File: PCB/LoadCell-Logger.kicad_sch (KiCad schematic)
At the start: 71 parts, among them CN2 LoadCell, CN3 LoadCell, CN4 LoadCell, Q2 MMBT3906, Q3 MMBT3906, Q4 MMBT3906, SW2 Reset, U1 Pico, U2 TC74HCU04AF, U3 HX711, U4 HX711, U5 HX711, U6 HX711, U7 Pico

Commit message: 部品配置
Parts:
- C1, C10, C12, C13, C15, C17, C18, C20, C22, C3, C7, C8: footprint (none) -> Capacitor_SMD:C_0603_1608Metric_Pad1.08x0.95mm_HandSolder
- C11, C14, C16, C19, C21, C9: footprint (none) -> Capacitor_SMD:C_0805_2012Metric_Pad1.18x1.45mm_HandSolder
- C2: value (none) -> 10p; footprint (none) -> Capacitor_SMD:C_0603_1608Metric_Pad1.08x0.95mm_HandSolder
- C4, C6: value (none) -> 10u; footprint (none) -> Capacitor_SMD:C_0805_2012Metric_Pad1.18x1.45mm_HandSolder
- C5: value (none) -> 0.1u; footprint (none) -> Capacitor_SMD:C_0603_1608Metric_Pad1.08x0.95mm_HandSolder
- CN1: value (none) -> LoadCell; footprint (none) -> Connector_Molex:Molex_SPOX_5268-04A_1x04_P2.50mm_Horizontal
- CN2, CN3, CN4: footprint (none) -> Connector_Molex:Molex_SPOX_5268-04A_1x04_P2.50mm_Horizontal
- D1: value (none) -> LED; footprint (none) -> LED_SMD:LED_0603_1608Metric_Pad1.05x0.95mm_HandSolder
- D2, D3, D4: footprint (none) -> LED_SMD:LED_0603_1608Metric_Pad1.05x0.95mm_HandSolder
- J1: value (none) -> Debug; footprint (none) -> user:STlink
- J2: value (none) -> Debug_Power; footprint (none) -> Connector_JST:JST_XH_S2B-XH-A_1x02_P2.50mm_Horizontal
- J3: value (none) -> Debug_XH; footprint (none) -> Connector_JST:JST_XH_S5B-XH-A_1x05_P2.50mm_Horizontal
- L1: value (none) -> BLM18RK102; footprint (none) -> Inductor_SMD:L_0603_1608Metric_Pad1.05x0.95mm_HandSolder
- Q1: value (none) -> MMBT3906; footprint (none) -> Package_TO_SOT_SMD:SOT-23
- R1: footprint (none) -> Resistor_SMD:R_0805_2012Metric_Pad1.20x1.40mm_HandSolder
- R10, R11, R12, R13, R14, R15, R16, R17, R18, R20, R21, R22, R6, R7, R8, R9: footprint (none) -> Resistor_SMD:R_0603_1608Metric_Pad0.98x0.95mm_HandSolder
- R19: value (none) -> 1k; footprint (none) -> Resistor_SMD:R_0603_1608Metric_Pad0.98x0.95mm_HandSolder
- R2: value (none) -> 300; footprint (none) -> Resistor_SMD:R_0603_1608Metric_Pad0.98x0.95mm_HandSolder
- R3: value (none) -> 22k; footprint (none) -> Resistor_SMD:R_0603_1608Metric_Pad0.98x0.95mm_HandSolder
- R4: value (none) -> 10k; footprint (none) -> Resistor_SMD:R_0603_1608Metric_Pad0.98x0.95mm_HandSolder
- R5: value (none) -> 100; footprint (none) -> Resistor_SMD:R_0603_1608Metric_Pad0.98x0.95mm_HandSolder
- SW1: value (none) -> User; footprint (none) -> user:SKRPACE010_kai
- SW2: footprint (none) -> user:SKRPACE010_kai
- SW3: value (none) -> SW_SPDT; footprint (none) -> user:SSSS213202_parallel
- U1, U7: footprint (none) -> MCU_RaspberryPi_and_Boards:RPi_Pico_SMD_TH
- U2: footprint (none) -> Package_SO:SO-14_5.3x10.2mm_P1.27mm
- U3, U4, U5, U6: footprint (none) -> Package_SO:SOP-16_3.9x9.9mm_P1.27mm
- Y1: value (none) -> 13.824MHz; footprint (none) -> Crystal:Crystal_HC49-U_Vertical
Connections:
- net CLK1: now also U2.2; no longer U2.6
- net GND: now also J1.5 (Pin_5); no longer C10.2, C11.1, C14.2, C15.2, C16.1, C19.2, C20.2, C21.1, C4.2, C5.2, C6.1, C9.2, CN1.2 (Pin_2), CN2.2 (Pin_2), CN3.2 (Pin_2), CN4.2 (Pin_2), R12.2, R16.2, R4.2, R8.2, U3.5 (AGND), U4.5 (AGND), U5.5 (AGND), U6.5 (AGND)
- net at R1.2, R2.2: now also U2.4, U2.5; no longer U2.2, U2.3
- net at C1.1, R1.1, Y1.1: now also U2.3; no longer U2.1
- net at U2.11, U2.13, U2.9: now also U2.1, U2.6; no longer U2.4, U2.5
- new net GNDA: C10.2, C11.1, C14.2, C15.2, C16.1, C19.2, C20.2, C21.1, C4.2, C5.2, C6.1, C9.2, CN1.2 (Pin_2), CN2.2 (Pin_2), CN3.2 (Pin_2), CN4.2 (Pin_2), R12.2, R16.2, R4.2, R8.2, U3.5 (AGND), U4.5 (AGND), U5.5 (AGND), U6.5 (AGND)
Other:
- moved on the sheet: U2A, U2B, U2C

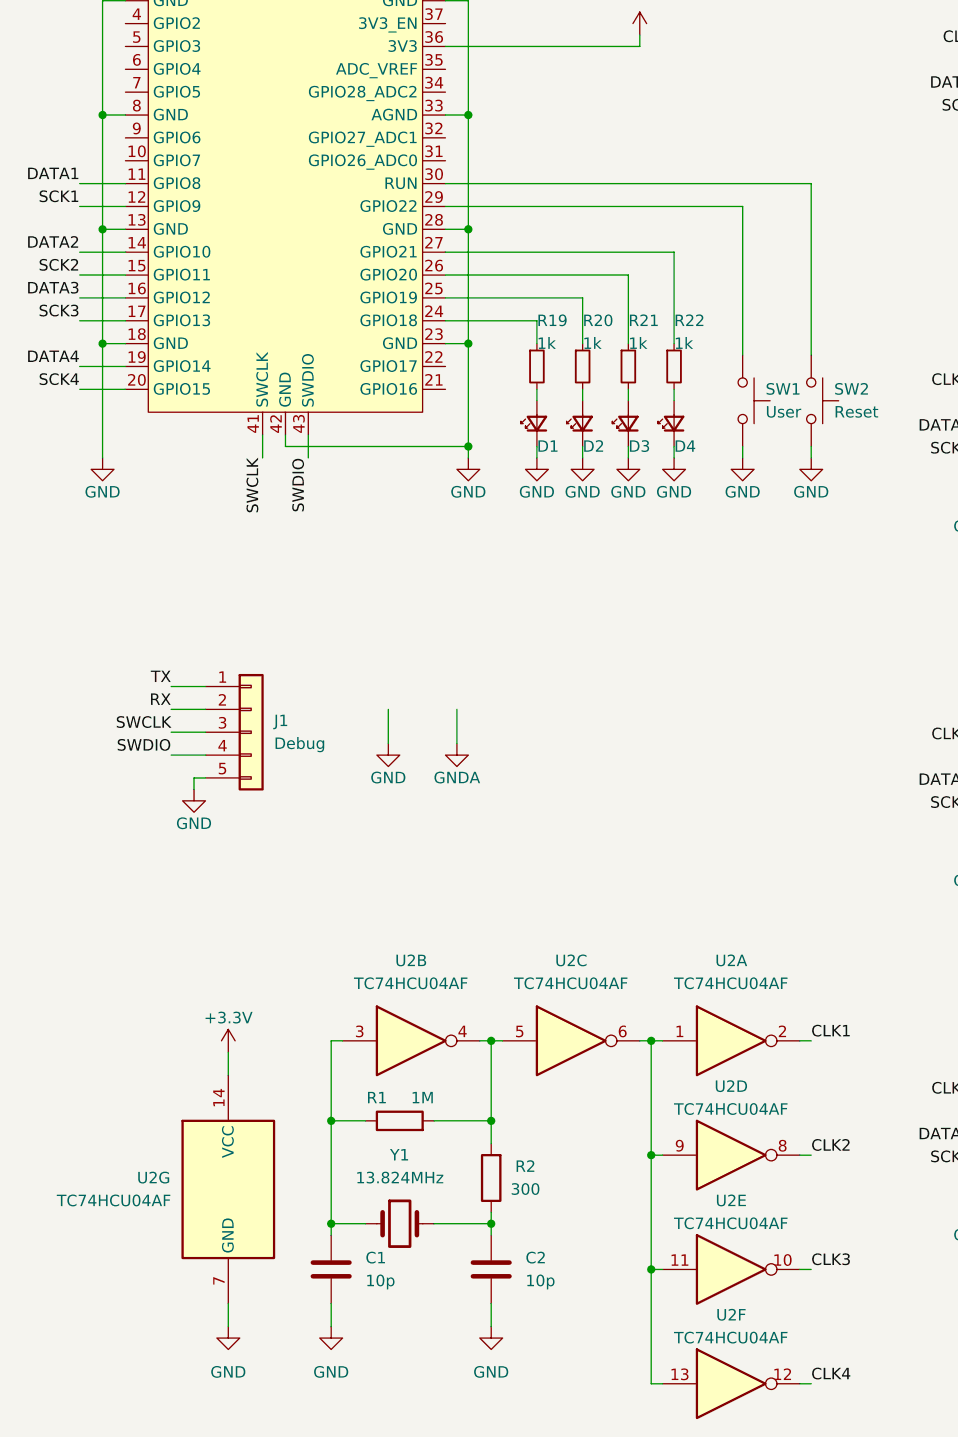
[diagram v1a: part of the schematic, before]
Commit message: ロガー側配線完了
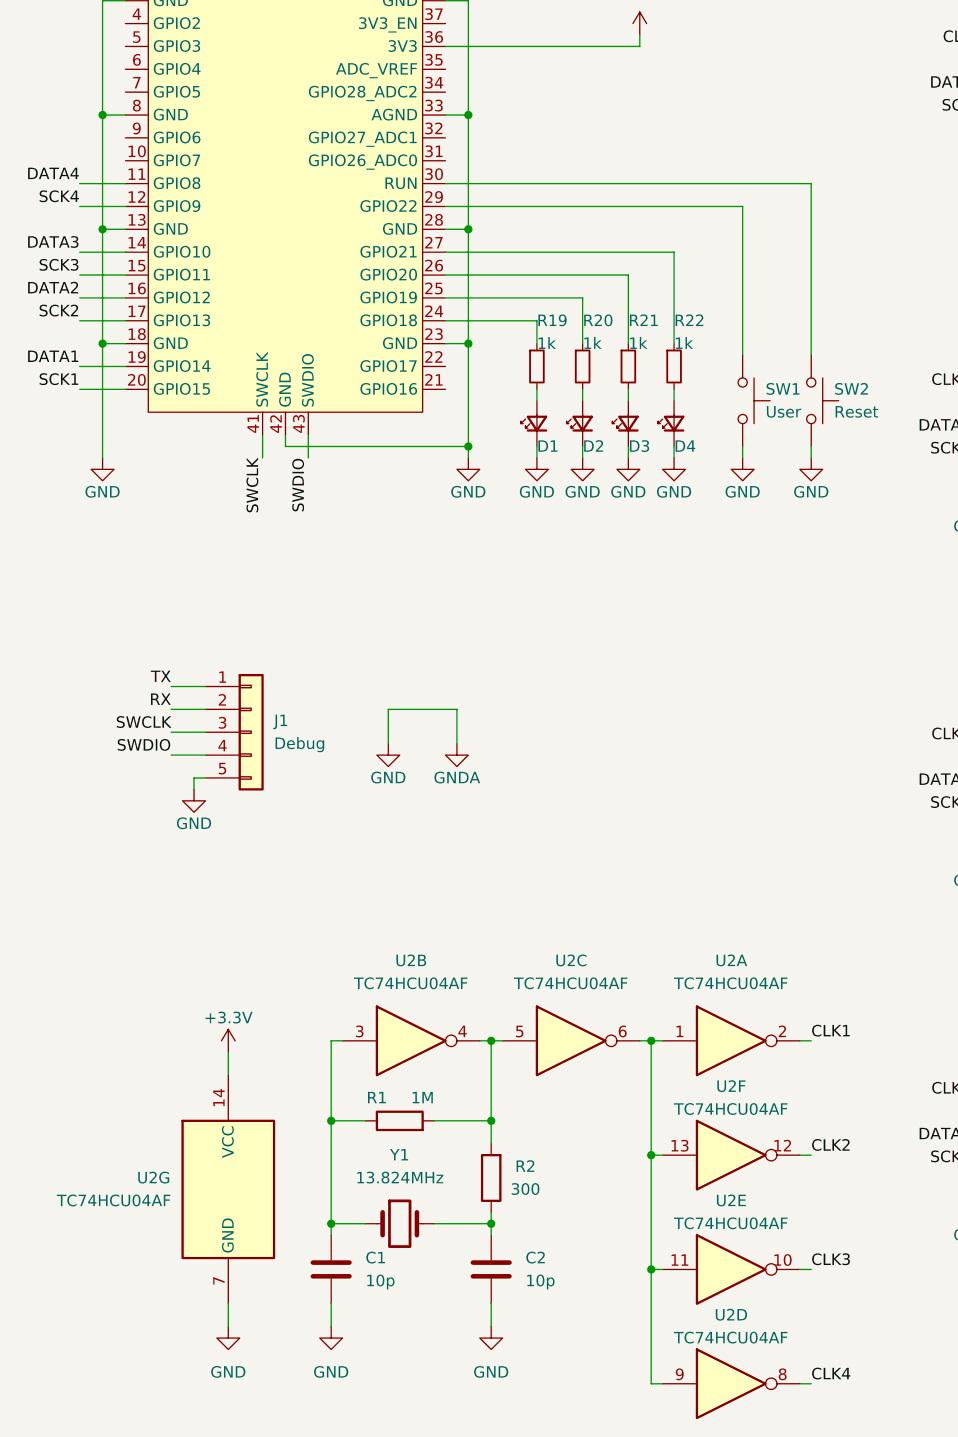
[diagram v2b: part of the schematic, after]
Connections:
- net GNDA is gone; now on net GND: C10.2, C11.1, C14.2, C15.2, C16.1, C19.2, C20.2, C21.1, C4.2, C5.2, C6.1, C9.2, CN1.2 (Pin_2), CN2.2 (Pin_2), CN3.2 (Pin_2), CN4.2 (Pin_2), R12.2, R16.2, R4.2, R8.2, U3.5 (AGND), U4.5 (AGND), U5.5 (AGND), U6.5 (AGND)
- net CLK2: now also U2.12; no longer U2.8
- net CLK4: now also U2.8; no longer U2.12
- net DATA1: now also U1.19 (GPIO14); no longer U1.11 (GPIO8)
- net DATA2: now also U1.16 (GPIO12); no longer U1.14 (GPIO10)
- net DATA3: now also U1.14 (GPIO10); no longer U1.16 (GPIO12)
- net DATA4: now also U1.11 (GPIO8); no longer U1.19 (GPIO14)
- net SCK1: now also U1.20 (GPIO15); no longer U1.12 (GPIO9)
- net SCK2: now also U1.17 (GPIO13); no longer U1.15 (GPIO11)
- net SCK3: now also U1.15 (GPIO11); no longer U1.17 (GPIO13)
- net SCK4: now also U1.12 (GPIO9); no longer U1.20 (GPIO15)
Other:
- moved on the sheet: U2D, U2F
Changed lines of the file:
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@@
+    (stroke (width 0) (type default) (color 0 0 0 0))
+  )
+  (wire (pts (xy 55.88 106.68) (xy 63.5 106.68))
     (stroke (width 0) (type default) (color 0 0 0 0))
   )
@@
     (effects (font (size 1.27 1.27)) (justify right bottom))
   )
-  (label "SCK1" (at 21.59 50.8 180)
+  (label "SCK4" (at 21.59 50.8 180)
     (effects (font (size 1.27 1.27)) (justify right bottom))
   )
@@
     (effects (font (size 1.27 1.27)) (justify right bottom))
   )
-  (label "DATA2" (at 21.59 55.88 180)
+  (label "DATA3" (at 21.59 55.88 180)
     (effects (font (size 1.27 1.27)) (justify right bottom))
   )
@@
     (effects (font (size 1.27 1.27)) (justify right bottom))
   )
-  (label "DATA4" (at 21.59 68.58 180)
+  (label "DATA1" (at 21.59 68.58 180)
     (effects (font (size 1.27 1.27)) (justify right bottom))
   )
@@
     (effects (font (size 1.27 1.27)) (justify right bottom))
   )
-  (label "SCK2" (at 21.59 58.42 180)
-    (effects (font (size 1.27 1.27)) (justify right bottom))
-  )
-  (label "SCK4" (at 21.59 71.12 180)
+  (label "SCK3" (at 21.59 58.42 180)
+    (effects (font (size 1.27 1.27)) (justify right bottom))
+  )
+  (label "SCK1" (at 21.59 71.12 180)
     (effects (font (size 1.27 1.27)) (justify right bottom))
   )
@@
     (effects (font (size 1.27 1.27)) (justify right bottom))
   )
-  (label "DATA3" (at 21.59 60.96 180)
+  (label "DATA2" (at 21.59 60.96 180)
     (effects (font (size 1.27 1.27)) (justify right bottom))
   )
@@
     (effects (font (size 1.27 1.27)) (justify right bottom))
   )
-  (label "DATA1" (at 21.59 48.26 180)
+  (label "DATA4" (at 21.59 48.26 180)
     (effects (font (size 1.27 1.27)) (justify right bottom))
   )
@@
     (effects (font (size 1.27 1.27)) (justify right bottom))
   )
-  (label "SCK3" (at 21.59 63.5 180)
+  (label "SCK2" (at 21.59 63.5 180)
     (effects (font (size 1.27 1.27)) (justify right bottom))
   )
@@
   (symbol (lib_id "power:GND") (at 34.29 115.57 0) (unit 1)
     (in_bom yes) (on_board yes)
-    (property "Reference" "#PWR?" (id 0) (at 34.29 121.92 0)
+    (property "Reference" "#PWR0101" (id 0) (at 34.29 121.92 0)
       (effects (font (size 1.27 1.27)) hide)
     )
@@
     (pin "2")
   )
-  (symbol (lib_id "74xx:74HC04") (at 93.98 181.61 0) (unit 6)
-    (in_bom yes) (on_board yes)
-    (property "Reference" "U2" (id 0) (at 93.98 173.99 0))
-    (property "Value" "TC74HCU04AF" (id 1) (at 93.98 176.53 0))
-    (property "Footprint" "Package_SO:SO-14_5.3x10.2mm_P1.27mm" (id 2) (at 93.98 181.61 0)
-      (effects (font (size 1.27 1.27)) hide)
-    )
-    (property "Datasheet" "https://assets.nexperia.com/documents/data-sheet/74HC_HCT04.pdf" (id 3) (at 93.98 181.61 0)
+  (symbol (lib_id "74xx:74HC04") (at 93.98 156.21 0) (unit 6)
+    (in_bom yes) (on_board yes)
+    (property "Reference" "U2" (id 0) (at 93.98 148.59 0))
+    (property "Value" "TC74HCU04AF" (id 1) (at 93.98 151.13 0))
+    (property "Footprint" "Package_SO:SO-14_5.3x10.2mm_P1.27mm" (id 2) (at 93.98 156.21 0)
+      (effects (font (size 1.27 1.27)) hide)
+    )
+    (property "Datasheet" "https://assets.nexperia.com/documents/data-sheet/74HC_HCT04.pdf" (id 3) (at 93.98 156.21 0)
       (effects (font (size 1.27 1.27)) hide)
     )
@@
     (pin "3")
   )
-  (symbol (lib_id "74xx:74HC04") (at 93.98 156.21 0) (unit 4)
-    (in_bom yes) (on_board yes)
-    (property "Reference" "U2" (id 0) (at 93.98 148.59 0))
-    (property "Value" "TC74HCU04AF" (id 1) (at 93.98 151.13 0))
-    (property "Footprint" "Package_SO:SO-14_5.3x10.2mm_P1.27mm" (id 2) (at 93.98 156.21 0)
-      (effects (font (size 1.27 1.27)) hide)
-    )
-    (property "Datasheet" "https://assets.nexperia.com/documents/data-sheet/74HC_HCT04.pdf" (id 3) (at 93.98 156.21 0)
+  (symbol (lib_id "74xx:74HC04") (at 93.98 181.61 0) (unit 4)
+    (in_bom yes) (on_board yes)
+    (property "Reference" "U2" (id 0) (at 93.98 173.99 0))
+    (property "Value" "TC74HCU04AF" (id 1) (at 93.98 176.53 0))
+    (property "Footprint" "Package_SO:SO-14_5.3x10.2mm_P1.27mm" (id 2) (at 93.98 181.61 0)
+      (effects (font (size 1.27 1.27)) hide)
+    )
+    (property "Datasheet" "https://assets.nexperia.com/documents/data-sheet/74HC_HCT04.pdf" (id 3) (at 93.98 181.61 0)
       (effects (font (size 1.27 1.27)) hide)
     )
@@
     )
     (path "/76fca29f-1432-45fd-a75f-490560bc3c42"
-      (reference "#PWR?") (unit 1) (value "GND") (footprint "")
+      (reference "#PWR0101") (unit 1) (value "GND") (footprint "")
     )
     (path "/8ee23804-ba2e-43bb-a051-a3738fd405c2"

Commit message: 基板設計完了
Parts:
- added SW2: (no value), user:SKRPACE010_kai, symbol Switch:SW_Push
- SW1: value User -> (none)
- renumbered SW2 to SW3, SW3 to SW4
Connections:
- net SWCLK is gone; now on net CLK: J1.3 (Pin_3), U1.41 (SWCLK)
- net SWDIO is gone; now on net DIO: J1.4 (Pin_4), U1.43 (SWDIO)
- net GND: now also SW2.2
- net at U1.31 (GPIO26_ADC0): now also SW2.1
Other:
- moved on the sheet: SW3
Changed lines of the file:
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@@
   (no_connect (at 125.73 73.66))
   (no_connect (at 127 35.56))
-  (wire (pts (xy 102.87 77.47) (xy 102.87 78.74))
+  (wire (pts (xy 107.95 58.42) (xy 107.95 59.69))
     (stroke (width 0) (type default) (color 0 0 0 0))
   )
@@
     (stroke (width 0) (type default) (color 0 0 0 0))
   )
-  (wire (pts (xy 62.23 48.26) (xy 102.87 48.26))
+  (wire (pts (xy 62.23 48.26) (xy 107.95 48.26))
     (stroke (width 0) (type default) (color 0 0 0 0))
   )
@@
     (stroke (width 0) (type default) (color 0 0 0 0))
   )
-  (wire (pts (xy 102.87 48.26) (xy 102.87 67.31))
-    (stroke (width 0) (type default) (color 0 0 0 0))
-  )
   (wire (pts (xy 148.59 60.96) (xy 149.86 60.96))
     (stroke (width 0) (type default) (color 0 0 0 0))
@@
     (stroke (width 0) (type default) (color 0 0 0 0))
   )
+  (wire (pts (xy 234.95 134.62) (xy 243.84 134.62))
+    (stroke (width 0) (type default) (color 0 0 0 0))
+  )
   (wire (pts (xy 49.53 152.4) (xy 49.53 163.83))
     (stroke (width 0) (type default) (color 0 0 0 0))
@@
     (stroke (width 0) (type default) (color 0 0 0 0))
   )
+  (wire (pts (xy 234.95 132.08) (xy 243.84 132.08))
+    (stroke (width 0) (type default) (color 0 0 0 0))
+  )
   (wire (pts (xy 278.13 81.28) (xy 278.13 26.67))
     (stroke (width 0) (type default) (color 0 0 0 0))
@@
     (stroke (width 0) (type default) (color 0 0 0 0))
   )
+  (wire (pts (xy 62.23 45.72) (xy 102.87 45.72))
+    (stroke (width 0) (type default) (color 0 0 0 0))
+  )
   (wire (pts (xy 120.65 78.74) (xy 125.73 78.74))
     (stroke (width 0) (type default) (color 0 0 0 0))
@@
     (stroke (width 0) (type default) (color 0 0 0 0))
   )
+  (wire (pts (xy 102.87 45.72) (xy 102.87 67.31))
+    (stroke (width 0) (type default) (color 0 0 0 0))
+  )
   (wire (pts (xy 158.75 118.11) (xy 172.72 118.11))
     (stroke (width 0) (type default) (color 0 0 0 0))
@@
     (stroke (width 0) (type default) (color 0 0 0 0))
   )
+  (wire (pts (xy 102.87 77.47) (xy 102.87 78.74))
+    (stroke (width 0) (type default) (color 0 0 0 0))
+  )
   (wire (pts (xy 147.32 152.4) (xy 163.83 152.4))
     (stroke (width 0) (type default) (color 0 0 0 0))
@@
     (effects (font (size 1.27 1.27)) (justify right bottom))
   )
+  (label "DIO" (at 243.84 134.62 180)
+    (effects (font (size 1.27 1.27)) (justify right bottom))
+  )
   (label "SWDIO" (at 46.99 78.74 270)
     (effects (font (size 1.27 1.27)) (justify right bottom))
@@
     (effects (font (size 1.27 1.27)) (justify right bottom))
   )
+  (label "SWDIO" (at 234.95 134.62 180)
+    (effects (font (size 1.27 1.27)) (justify right bottom))
+  )
   (label "DATA3" (at 21.59 55.88 180)
     (effects (font (size 1.27 1.27)) (justify right bottom))
@@
     (effects (font (size 1.27 1.27)) (justify right bottom))
   )
+  (label "SWCLK" (at 234.95 132.08 180)
+    (effects (font (size 1.27 1.27)) (justify right bottom))
+  )
   (label "SCK1" (at 21.59 71.12 180)
     (effects (font (size 1.27 1.27)) (justify right bottom))
@@
     (effects (font (size 1.27 1.27)) (justify right bottom))
   )
+  (label "CLK" (at 243.84 132.08 180)
+    (effects (font (size 1.27 1.27)) (justify right bottom))
+  )
   (label "TX" (at 31.75 104.14 180)
     (effects (font (size 1.27 1.27)) (justify right bottom))
@@
       (effects (font (size 1.27 1.27)) (justify left))
     )
-    (property "Value" "User" (id 1) (at 97.79 73.66 90)
+    (property "Value" "" (id 1) (at 97.79 73.66 90)
       (effects (font (size 1.27 1.27)) (justify left))
     )
@@
     (pin "2")
   )
-  (symbol (lib_id "power:GND") (at 102.87 78.74 0) (unit 1)
+  (symbol (lib_id "power:GND") (at 107.95 59.69 0) (unit 1)
     (in_bom yes) (on_board yes)
-    (property "Reference" "#PWR041" (id 0) (at 102.87 85.09 0)
+    (property "Reference" "#PWR041" (id 0) (at 107.95 66.04 0)
       (effects (font (size 1.27 1.27)) hide)
     )
-    (property "Value" "GND" (id 1) (at 102.87 82.55 0))
-    (property "Footprint" "" (id 2) (at 102.87 78.74 0)
+    (property "Value" "GND" (id 1) (at 107.95 63.5 0))
+    (property "Footprint" "" (id 2) (at 107.95 59.69 0)
       (effects (font (size 1.27 1.27)) hide)
     )
-    (property "Datasheet" "" (id 3) (at 102.87 78.74 0)
+    (property "Datasheet" "" (id 3) (at 107.95 59.69 0)
       (effects (font (size 1.27 1.27)) hide)
     )
@@
     (pin "1")
   )
-  (symbol (lib_id "Switch:SW_Push") (at 102.87 72.39 270) (unit 1)
+  (symbol (lib_id "Switch:SW_Push") (at 107.95 53.34 270) (unit 1)
     (in_bom yes) (on_board yes)
-    (property "Reference" "SW2" (id 0) (at 105.41 71.12 90)
+    (property "Reference" "SW3" (id 0) (at 110.49 52.07 90)
       (effects (font (size 1.27 1.27)) (justify left))
     )
-    (property "Value" "Reset" (id 1) (at 105.41 73.66 90)
+    (property "Value" "Reset" (id 1) (at 110.49 54.61 90)
       (effects (font (size 1.27 1.27)) (justify left))
     )
-    (property "Footprint" "user:SKRPACE010_kai" (id 2) (at 107.95 72.39 0)
+    (property "Footprint" "user:SKRPACE010_kai" (id 2) (at 113.03 53.34 0)
       (effects (font (size 1.27 1.27)) hide)
     )
-    (property "Datasheet" "~" (id 3) (at 107.95 72.39 0)
+    (property "Datasheet" "~" (id 3) (at 113.03 53.34 0)
       (effects (font (size 1.27 1.27)) hide)
     )
@@
     (pin "2")
   )
+  (symbol (lib_id "Switch:SW_Push") (at 102.87 72.39 270) (unit 1)
+    (in_bom yes) (on_board yes)
+    (property "Reference" "SW2" (id 0) (at 105.41 71.12 90)
+      (effects (font (size 1.27 1.27)) (justify left))
+    )
+    (property "Value" "" (id 1) (at 105.41 73.66 90)
+      (effects (font (size 1.27 1.27)) (justify left))
+    )
+    (property "Footprint" "user:SKRPACE010_kai" (id 2) (at 107.95 72.39 0)
+      (effects (font (size 1.27 1.27)) hide)
+    )
+    (property "Datasheet" "~" (id 3) (at 107.95 72.39 0)
+      (effects (font (size 1.27 1.27)) hide)
+    )
+    (pin "1")
+    (pin "2")
+  )
   (symbol (lib_id "Device:C_Small") (at 156.21 118.11 90) (unit 1)
     (in_bom yes) (on_board yes)
@@
   (symbol (lib_id "Switch:SW_SPDT") (at 265.43 88.9 90) (unit 1)
     (in_bom yes) (on_board yes)
-    (property "Reference" "SW3" (id 0) (at 257.81 88.9 90)
+    (property "Reference" "SW4" (id 0) (at 257.81 88.9 90)
       (effects (font (size 1.27 1.27)) (justify right))
     )
@@
     (pin "2")
   )
+  (symbol (lib_id "power:GND") (at 102.87 78.74 0) (unit 1)
+    (in_bom yes) (on_board yes)
+    (property "Reference" "#PWR0102" (id 0) (at 102.87 85.09 0)
+      (effects (font (size 1.27 1.27)) hide)
+    )
+    (property "Value" "GND" (id 1) (at 102.87 82.55 0))
+    (property "Footprint" "" (id 2) (at 102.87 78.74 0)
+      (effects (font (size 1.27 1.27)) hide)
+    )
+    (property "Datasheet" "" (id 3) (at 102.87 78.74 0)
+      (effects (font (size 1.27 1.27)) hide)
+    )
+    (pin "1")
+  )
   (symbol (lib_id "power:GND") (at 274.32 82.55 0) (unit 1)
     (in_bom yes) (on_board yes)
@@
       (reference "#PWR0101") (unit 1) (value "GND") (footprint "")
     )
+    (path "/fbed80b1-027c-4537-a82c-ef76985a210a"
+      (reference "#PWR0102") (unit 1) (value "GND") (footprint "")
+    )
     (path "/8ee23804-ba2e-43bb-a051-a3738fd405c2"
       (reference "C1") (unit 1) (value "10p") (footprint "Capacitor_SMD:C_0603_1608Metric_Pad1.08x0.95mm_HandSolder")
@@
     )
     (path "/35808532-6a93-4465-8818-ecfa04009b20"
-      (reference "SW1") (unit 1) (value "User") (footprint "user:SKRPACE010_kai")
+      (reference "SW1") (unit 1) (value "A") (footprint "user:SKRPACE010_kai")
+    )
+    (path "/b9c81503-471d-4914-9fd1-d3fd081c064d"
+      (reference "SW2") (unit 1) (value "B") (footprint "user:SKRPACE010_kai")
     )
     (path "/891aa474-e005-46d2-89e6-1259c71502ed"
-      (reference "SW2") (unit 1) (value "Reset") (footprint "user:SKRPACE010_kai")
+      (reference "SW3") (unit 1) (value "Reset") (footprint "user:SKRPACE010_kai")
     )
     (path "/d36eae44-016d-4006-bbf9-932a060b8508"
-      (reference "SW3") (unit 1) (value "SW_SPDT") (footprint "user:SSSS213202_parallel")
+      (reference "SW4") (unit 1) (value "SW_SPDT") (footprint "user:SSSS213202_parallel")
     )
     (path "/e0c7ddff-8c90-465f-be62-21fb49b059fa"
